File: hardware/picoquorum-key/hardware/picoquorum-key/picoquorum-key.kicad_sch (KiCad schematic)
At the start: 52 parts, among them J1 USB-C, J2 ST7789 1.14in panel, Q1 AO3401A, Q2 MMBT3904, SW1 D0 Reject, SW2 D1 Next, SW3 D2 Sign, SW6 BOOT, SW7 RESET, U1 ESP32-S3-WROOM-1-N8R2, U2 ATECC608C-MAHDA, U3 AMS1117-3.3, U4 USBLC6-2SC6

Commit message: picoquorum-key rev B: an optional key port for a key-c
Adds a straddle USB-C plug (C3151751) at the board's top-left corner, on a
0.8 mm board widened 6 mm to 50 x 53. The key-c gets an I2C bus of its own
(GPIO38/39) and power through an AP22653 switch whose EN is pulled down, so
the key is off at reset and under any image that doesn't know the port. The
port also has CC on GPIO1 (R17 47k on every board), ESD on every plug line,
and a TVS on VKEY.

Departures from the plan:
- No LED or FAULT pins. Rev A's routing closes in module pins 21 and 24.
  D4 and a key-c P3's LED run off VKEY, and U5's FAULT is left open.
- The ESP32 module footprint's 48 mm keep-out is removed. The antenna rule
  area is now the module's antenna end plus 0.5 mm.

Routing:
- Rev A's routing is copied, moved 6 mm and locked (seed_route.py), and
  Freerouting routes only the port's connections.
- finish_route.py routes the few connections it left open.
- One GND via by U6 was placed by hand.

Fit groups: bom.csv/cpl.csv for base boards, bom-port.csv/cpl-port.csv
with the port's parts. The Gerbers are the same for both.

Checks:
- ERC 0; DRC 0 violations, 0 unconnected, 0 parity.
- tools/test.sh: 161 tests, 11 skipped (test_3d: no FreeCAD here).
- Visual goldens re-approved (KiCad 10.0.7).

The console image (firmware/board.py) is unchanged: only this board's
profile constants, PINS.md and smoke test know the port.

Co-Authored-By: Claude Opus 5.5 <noreply@anthropic.com>
Claude-Session: https://claude.ai/code/session_01H2mKC2z3aivAd8yF8tbg6X
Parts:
- added C10: 10u, Capacitor_SMD:C_0805_2012Metric, symbol Device:C
- added C9: 100n, Capacitor_SMD:C_0603_1608Metric, symbol Device:C
- added D3: ESD5Z5V0, Diode_SMD:D_SOD-523, symbol Diode:ESD5Zxx
- added D4: green, LED_SMD:LED_0603_1608Metric, symbol Device:LED
- added J3: USB-C plug, straddle, console:USB_C_Plug_ShouHan_24P-GTJB_Straddle, symbol console:USB_C_Plug_Straddle
- added R15: 100k, Resistor_SMD:R_0603_1608Metric, symbol Device:R
- added R17: 47k, Resistor_SMD:R_0603_1608Metric, symbol Device:R
- added R18, R22: 1k, Resistor_SMD:R_0603_1608Metric, symbol Device:R
- added R19, R20: 2.2k, Resistor_SMD:R_0603_1608Metric, symbol Device:R
- added R21: 100, Resistor_SMD:R_0603_1608Metric, symbol Device:R
- added TP13: KEY2_SDA, TestPoint:TestPoint_Pad_1.5x1.5mm, symbol Connector:TestPoint
- added TP14: KEY2_SCL, TestPoint:TestPoint_Pad_1.5x1.5mm, symbol Connector:TestPoint
- added U5: AP22653W6-7, Package_TO_SOT_SMD:SOT-23-6, symbol console:AP22653
- added U6, U7: USBLC6-2SC6, Package_TO_SOT_SMD:SOT-23-6, symbol Power_Protection:USBLC6-2SC6
- C1, C2, C3, C4, C5, C6, C7, C8, D1, H1, H2, H3, H4, J1, J2, Q1, Q2, R1, R10, R11, R12, R13, R14, R2, R3, R4, R5, R6, R7, R8, R9, SW1, SW2, SW3, SW6, SW7, TP1, TP11, TP12, TP2, TP3, TP4, TP5, TP6, TP7, TP8, U1, U2, U3, U4: Fit (none) -> base
- TP10: value IO2 -> KEY_EN; Fit (none) -> base; MPN IO2 -> KEY_EN
- TP9: value IO1 -> KEY_CC; Fit (none) -> base; MPN IO1 -> KEY_CC
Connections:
- net +3V3: now also C9.1, R17.1, U5.1 (IN), U6.5 (VBUS), U7.5 (VBUS)
- net GND: now also C10.2, C9.2, D3.2 (A), D4.1 (K), J3.A1 (GND), J3.A12 (GND), J3.B1 (GND), J3.B12 (GND), J3.SH (SHIELD), R15.2, U5.2 (GND), U5.5 (ILIM), U6.2 (GND), U7.2 (GND)
- net KEY2_SDA: now reaches U1.31 (IO38)
- net KEY2_SDA: now also J3.A6 (D+), R19.2, TP13.1, U6.1 (I/O1), U6.6 (I/O1)
- net KEY2_SCL: now reaches U1.32 (IO39)
- net KEY2_SCL: now also J3.A7 (D-), R20.2, TP14.1, U6.3 (I/O2), U6.4 (I/O2)
- net IO1 renamed KEY_CC
- net KEY_CC: now also R17.2, R18.1
- net IO2 renamed KEY_EN
- net KEY_EN: now also R15.1, U5.3 (EN)
- new net KEY_CC_PLUG: J3.A5 (CC), R18.2, U7.1 (I/O1), U7.6 (I/O1)
- new net KEY_LED_A: D4.2 (A), R22.2
- new net KEY_SBU: J3.A8 (SBU1), J3.B8 (SBU2), R21.2, U7.3 (I/O2), U7.4 (I/O2)
- new net VKEY: C10.1, D3.1 (K), J3.A4 (VBUS), J3.A9 (VBUS), J3.B4 (VBUS), J3.B9 (VBUS), R19.1, R20.1, R21.1, R22.1, U5.6 (OUT)
- no-connect marks 23 -> 33
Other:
- note added: "6 DEBUG PADS (back face) AND MOUNTING HOLES TP: 3V3 GND EN TX RX SDA SCL BOOT KCC KEN 5V GND KSDA KSCL"
- note added: "7 THE KEY PORT (rev B): a key-c on its own bus, I2C(1) Fit 'port' only, but R17 (every board). Power off at reset: R15 holds U5's EN low. SDA on D+ (A6), SCL on D- (A7), VKEY on VBUS, one CC line (A5), SBU (A8+B8) from VKEY. ESD rails on 3V3, never VKEY. J3 hand-fitted; 0.8 mm board."
- note removed: "6 DEBUG PADS (back face) AND MOUNTING HOLES TP: 3V3 GND EN TX RX SDA SCL BOOT IO1 IO2 5V GND"

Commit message: picoquorum-key rev B: D4 is D1's red LED (C2286)
The plan's green LED (C72043) is out of stock at JLCPCB. D4 is now the
red KT-0603R that D1 already uses: a basic part already on every order,
so no extra BOM line. At 3.3 V through R22 (1k) it gets about 1.4 mA, as
D1 does; the green InGaN part would have got under 1 mA.

Checks: ERC 0, DRC 0, tools/test.sh OK (11 skipped: no FreeCAD).

Co-Authored-By: Claude Opus 5.5 <noreply@anthropic.com>
Claude-Session: https://claude.ai/code/session_01H2mKC2z3aivAd8yF8tbg6X
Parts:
- D4: value green -> red; LCSC C72043 -> C2286; MPN 19-217/GHC-YR1S2/3T -> KT-0603R
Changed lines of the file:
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@@
 			)
 		)
-		(property "Value" "green"
+		(property "Value" "red"
 			(at 173.99 292.1 0)
 			(effects
@@
 			)
 		)
-		(property "LCSC" "C72043"
+		(property "LCSC" "C2286"
 			(at 177.8 297.18 0)
 			(effects
@@
 			)
 		)
-		(property "MPN" "19-217/GHC-YR1S2/3T"
+		(property "MPN" "KT-0603R"
 			(at 177.8 297.18 0)
 			(effects

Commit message: picoquorum-key rev B: D4 is a green KT-0603G (C12624)
Replaces the red C2286 stand-in. The plan's green C72043 is out of stock.
C12624's JLCPCB tier and stock weren't checked from here. At 3.3 V
through R22 (1k) a green LED gets under 1 mA; BRINGUP.md says to drop
R22 to 470 ohm if it is too dim.

Checks: ERC 0, DRC 0, tools/test.sh OK (11 skipped: no FreeCAD).

Co-Authored-By: Claude Opus 5.5 <noreply@anthropic.com>
Claude-Session: https://claude.ai/code/session_01H2mKC2z3aivAd8yF8tbg6X
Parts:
- D4: value red -> green; LCSC C2286 -> C12624; MPN KT-0603R -> KT-0603G
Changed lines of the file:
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@@
 			)
 		)
-		(property "Value" "red"
+		(property "Value" "green"
 			(at 173.99 292.1 0)
 			(effects
@@
 			)
 		)
-		(property "LCSC" "C2286"
+		(property "LCSC" "C12624"
 			(at 177.8 297.18 0)
 			(effects
@@
 			)
 		)
-		(property "MPN" "KT-0603R"
+		(property "MPN" "KT-0603G"
 			(at 177.8 297.18 0)
 			(effects

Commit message: picoquorum-key rev B: R22 470 ohm (C23179) for D4
The green KT-0603G drops about 2.7 V or more, so through 1k from VKEY it
got under 1 mA. 470 ohm gives about 1 mA. R22 is no longer on R18's 1k line,
so bom-port.csv has one line more.

Checks: ERC 0, DRC 0, tools/test.sh OK (11 skipped: no FreeCAD).

Co-Authored-By: Claude Opus 5.5 <noreply@anthropic.com>
Claude-Session: https://claude.ai/code/session_01H2mKC2z3aivAd8yF8tbg6X
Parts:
- R22: value 1k -> 470; LCSC C21190 -> C23179; MPN 1k -> 470
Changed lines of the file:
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@@
 			)
 		)
-		(property "Value" "1k"
+		(property "Value" "470"
 			(at 165.1 298.45 0)
 			(effects
@@
 			)
 		)
-		(property "LCSC" "C21190"
+		(property "LCSC" "C23179"
 			(at 162.56 297.18 0)
 			(effects
@@
 			)
 		)
-		(property "MPN" "1k"
+		(property "MPN" "470"
 			(at 162.56 297.18 0)
 			(effects

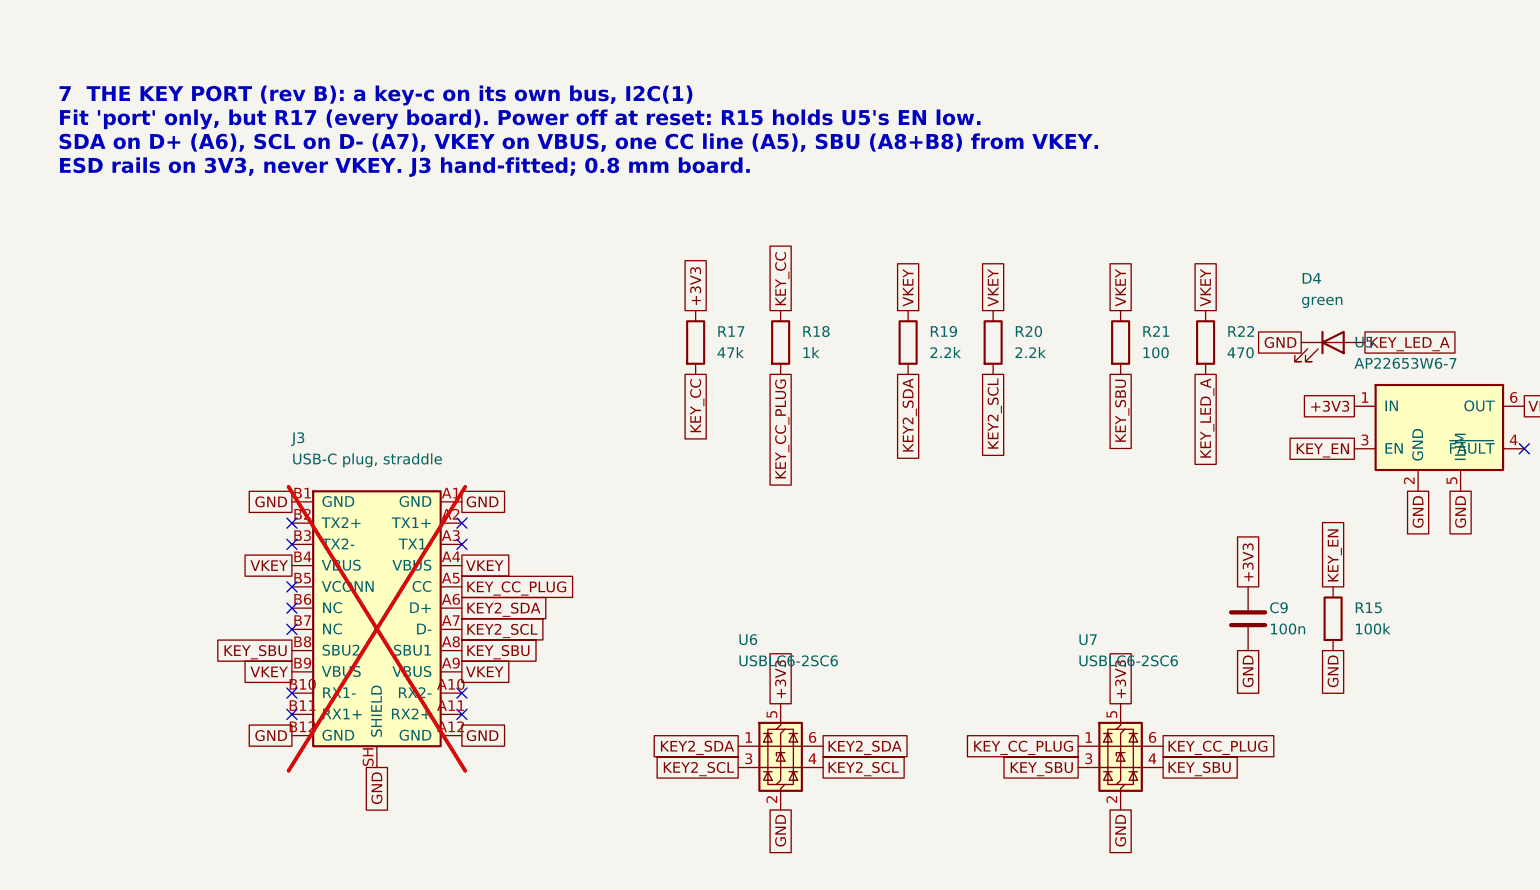
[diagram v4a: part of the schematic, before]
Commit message: picoquorum-key rev B: 5 V on the key port's VBUS no longer reaches 3V3 through SBU
U7's second channel was on SBU, which R21 (100 ohm) feeds from VKEY.
5 V put on the plug's VBUS then went R21 -> U7's diode -> 3V3, around
U5's reverse blocking: about 11 mA with the board on, enough to
half-power it when off. U7 now covers CC only; SBU meets only R21, so
D3 clamps it through 100 ohm. Its spur (3 vias, 13 segments) is gone
from the board; nothing else moved.

What is left is R19/R20 (2.2k) into U6's diodes and GPIO38/39's
clamps, about 0.5 mA a line. test_key_port holds the board to that,
and fails on the old circuit. BRINGUP.md gets a bench-supply check.

DESIGN.md's regulator note said the AMS1117 "wants >= 10 uF for
stability". Its datasheet asks for 22 uF of solid tantalum for all
conditions, allows smaller without an ADJ capacitor, and says nothing
about ceramics, which is all this board has. The note now says so,
with the heat sum, and BRINGUP.md scopes 3V3. The parts are unchanged.

ERC 0, DRC 0 with schematic parity. tools/test.sh: 162 tests, one
failure, test_3d's J3 without a model, as before. Fab files and the
approved pictures remade with KiCad 10.0.6 (they were 10.0.7's).

Co-Authored-By: Claude Opus 5.5 <noreply@anthropic.com>
Claude-Session: https://claude.ai/code/session_015Mrfds5ggPmPXMnhiEk5Pk
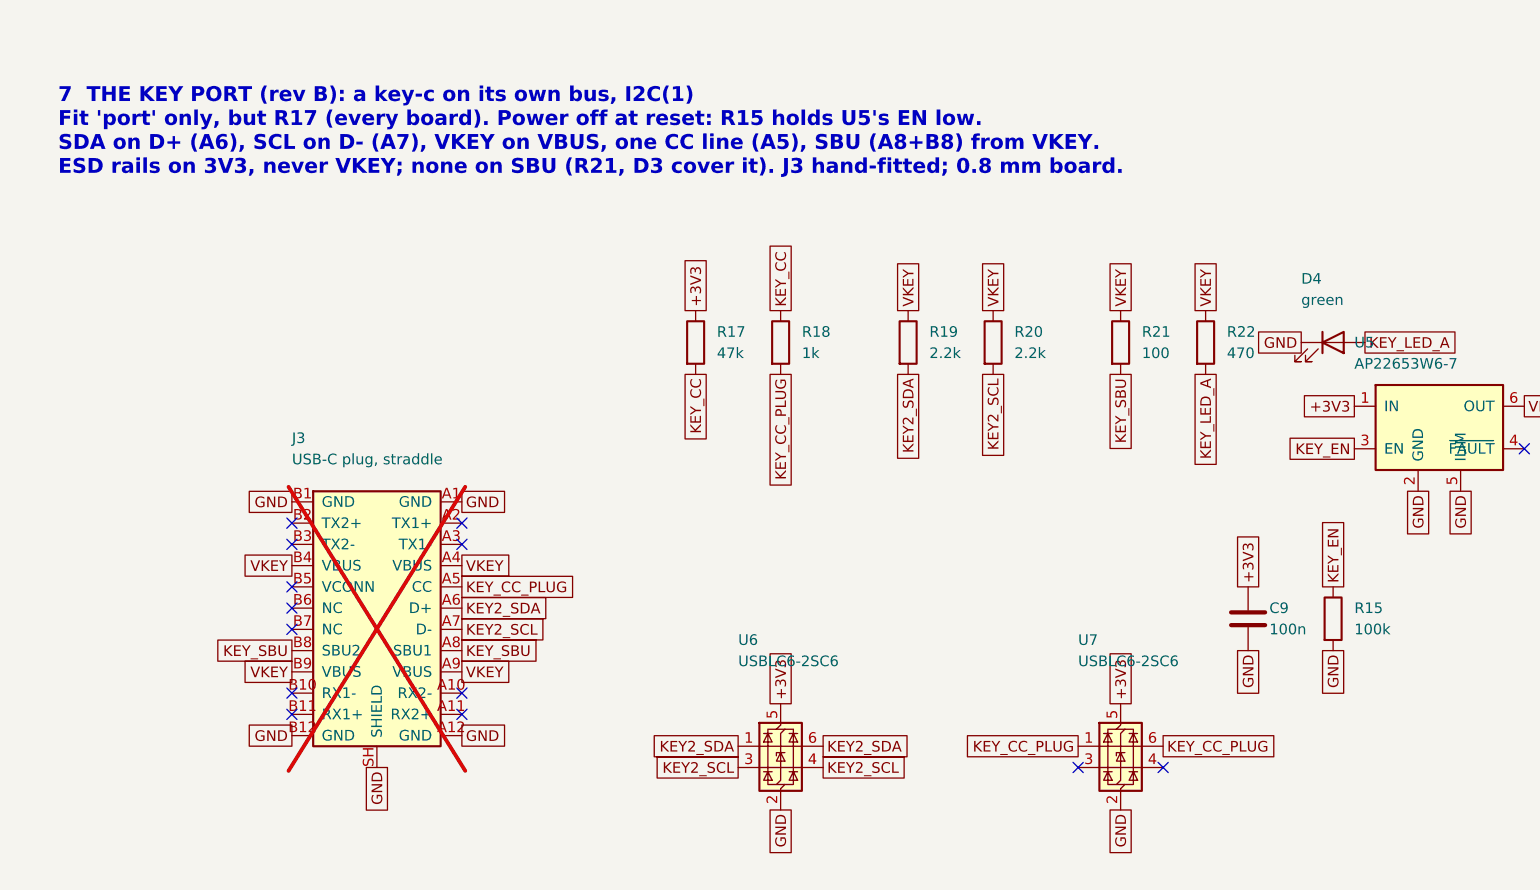
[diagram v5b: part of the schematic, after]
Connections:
- net KEY_SBU: no longer U7.3 (I/O2), U7.4 (I/O2)
- no-connect marks 33 -> 35
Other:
- note added: "7 THE KEY PORT (rev B): a key-c on its own bus, I2C(1) Fit 'port' only, but R17 (every board). Power off at reset: R15 holds U5's EN low. SDA on D+ (A6), SCL on D- (A7), VKEY on VBUS, one CC line (A5), SBU (A8+B8) from VKEY. ESD rails on 3V3, never VKEY; none on SBU (R21, D3 cover it). J3 hand-fitted; 0.8 mm board."
- note removed: "7 THE KEY PORT (rev B): a key-c on its own bus, I2C(1) Fit 'port' only, but R17 (every board). Power off at reset: R15 holds U5's EN low. SDA on D+ (A6), SCL on D- (A7), VKEY on VBUS, one CC line (A5), SBU (A8+B8) from VKEY. ESD rails on 3V3, never VKEY. J3 hand-fitted; 0.8 mm board."
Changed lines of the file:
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@@
 			)
 		)
-		(property "Description" "ESD on CC and the LED line (SBU), at the plug; its rail on 3V3"
+		(property "Description" "ESD on CC, at the plug; its rail on 3V3. Not on SBU: R21 would feed 5 V on VBUS into 3V3"
 			(at 152.4 345.44 0)
 			(effects
@@
 		)
 	)
-	(global_label "KEY_SBU"
-		(shape passive)
-		(at 147.32 347.98 180)
-		(fields_autoplaced yes)
-		(effects
-			(font
-				(size 1.27 1.27)
-			)
-			(justify right)
-		)
-		(property "Intersheetrefs" "${INTERSHEET_REFS}"
-			(at 147.32 347.98 0)
-			(effects
-				(font
-					(size 1.27 1.27)
-				)
-				(justify left)
-				(hide yes)
-			)
-		)
-	)
-	(global_label "KEY_SBU"
-		(shape passive)
-		(at 157.48 347.98 0)
+	(no_connect
+		(at 147.32 347.98)
+	)
+	(no_connect
+		(at 157.48 347.98)
+	)
+	(global_label "+3V3"
+		(shape passive)
+		(at 152.4 340.36 90)
 		(fields_autoplaced yes)
 		(effects
@@
 		)
 		(property "Intersheetrefs" "${INTERSHEET_REFS}"
-			(at 157.48 347.98 0)
-			(effects
-				(font
-					(size 1.27 1.27)
-				)
-				(justify left)
-				(hide yes)
-			)
-		)
-	)
-	(global_label "+3V3"
-		(shape passive)
-		(at 152.4 340.36 90)
+			(at 152.4 340.36 0)
+			(effects
+				(font
+					(size 1.27 1.27)
+				)
+				(justify left)
+				(hide yes)
+			)
+		)
+	)
+	(global_label "KEY_CC_PLUG"
+		(shape passive)
+		(at 157.48 345.44 0)
 		(fields_autoplaced yes)
 		(effects
@@
 		)
 		(property "Intersheetrefs" "${INTERSHEET_REFS}"
-			(at 152.4 340.36 0)
-			(effects
-				(font
-					(size 1.27 1.27)
-				)
-				(justify left)
-				(hide yes)
-			)
-		)
-	)
-	(global_label "KEY_CC_PLUG"
-		(shape passive)
-		(at 157.48 345.44 0)
-		(fields_autoplaced yes)
-		(effects
-			(font
-				(size 1.27 1.27)
-			)
-			(justify left)
-		)
-		(property "Intersheetrefs" "${INTERSHEET_REFS}"
 			(at 157.48 345.44 0)
 			(effects
@@
 		)
 	)
-	(text "7  THE KEY PORT (rev B): a key-c on its own bus, I2C(1)\nFit 'port' only, but R17 (every board). Power off at reset: R15 holds U5's EN low.\nSDA on D+ (A6), SCL on D- (A7), VKEY on VBUS, one CC line (A5), SBU (A8+B8) from VKEY.\nESD rails on 3V3, never VKEY. J3 hand-fitted; 0.8 mm board."
+	(text "7  THE KEY PORT (rev B): a key-c on its own bus, I2C(1)\nFit 'port' only, but R17 (every board). Power off at reset: R15 holds U5's EN low.\nSDA on D+ (A6), SCL on D- (A7), VKEY on VBUS, one CC line (A5), SBU (A8+B8) from VKEY.\nESD rails on 3V3, never VKEY; none on SBU (R21, D3 cover it). J3 hand-fitted; 0.8 mm board."
 		(exclude_from_sim no)
 		(at 25.4 266.7 0)
